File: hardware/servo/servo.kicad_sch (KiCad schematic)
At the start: 49 parts, among them J2 Conn_ARM_SWD_TagConnect_TC203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, U3 DRV8876PWPR, U4 STM32G030F6P6, U5 SIT3088EEUA, U6 SRV05-4

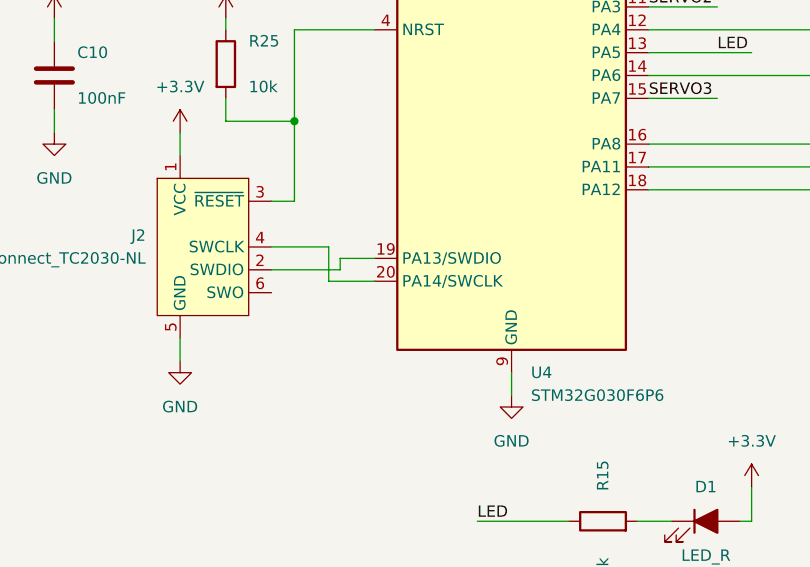
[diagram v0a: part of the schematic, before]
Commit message: hw/servo: add BOOT0 pull-down + test pad (same as ministepper)
STM32G030F6P6 on TSSOP-20 shares PA14 between SWCLK and the BOOT0
selector. Default option bytes read BOOT0 from the PA14 pin, so a
floating PA14 at cold boot (no debugger attached) can trigger an
unintended system-bootloader entry.

- R_BOOT0 (10k 0402, C25744) pull-down locks BOOT0 low at power-up
- TP_BOOT0 1x1mm solder pad for manual bootloader entry (short to
  +3V3 at reset to invoke system bootloader over USART1/RS-485 or
  I2C1)

Also embedded Connector:TestPoint in lib_symbols for BOM recognition.

Co-Authored-By: Claude Opus 4.6 (1M context) <noreply@anthropic.com>
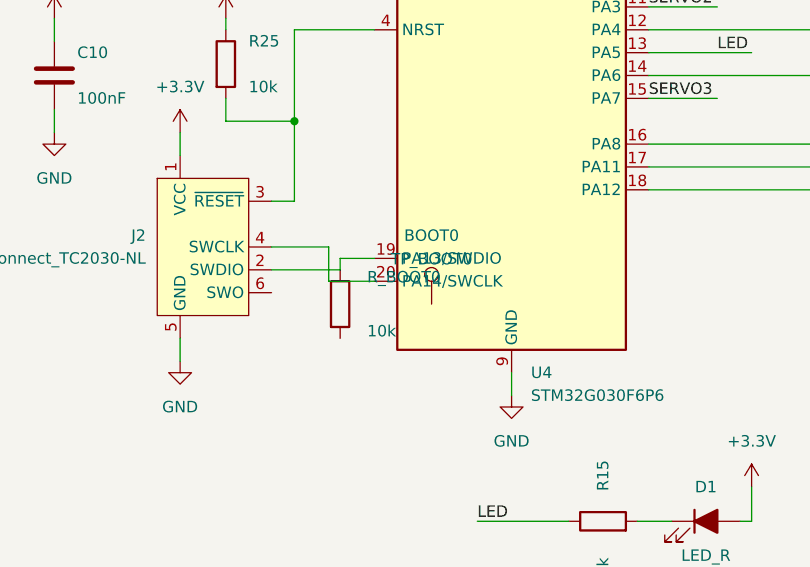
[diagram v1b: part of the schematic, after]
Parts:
- added R_BOOT0: 10k, Resistor_SMD:R_0402_1005Metric, symbol Device:R
- added TP_BOOT0: BOOT0, TestPoint:TestPoint_Pad_1.0x1.0mm, symbol Connector:TestPoint
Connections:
- net at J2.2 (SWDIO), U4.19 (PA13/SWDIO): now also R_BOOT0.1
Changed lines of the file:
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@@
+		)
+	)
+	(symbol
+		(lib_id "Device:R")
+		(at 201.93 166.37 0)
+		(unit 1)
+		(body_style 1)
+		(exclude_from_sim no)
+		(in_bom yes)
+		(on_board yes)
+		(in_pos_files yes)
+		(dnp no)
+		(uuid "b007bb01-1111-2222-3333-00000000r1ab")
+		(property "Reference" "R_BOOT0"
+			(at 204.93 163.37 0)
+			(show_name no)
+			(do_not_autoplace no)
+			(effects
+				(font
+					(size 1.27 1.27)
+				)
+				(justify left)
+			)
+		)
+		(property "Value" "10k"
+			(at 204.93 169.37 0)
+			(show_name no)
+			(do_not_autoplace no)
+			(effects
+				(font
+					(size 1.27 1.27)
+				)
+				(justify left)
+			)
+		)
+		(property "Footprint" "Resistor_SMD:R_0402_1005Metric"
+			(at 201.93 166.37 0)
+			(hide yes)
+			(show_name no)
+			(do_not_autoplace no)
+			(effects
+				(font
+					(size 1.27 1.27)
+				)
+			)
+		)
+		(property "Datasheet" ""
+			(at 201.93 166.37 0)
+			(hide yes)
+			(show_name no)
+			(do_not_autoplace no)
+			(effects
+				(font
+					(size 1.27 1.27)
+				)
+			)
+		)
+		(property "Description" "BOOT0 pull-down on PA14; locks cold boot to flash (BASIC)"
+			(at 201.93 166.37 0)
+			(hide yes)
+			(show_name no)
+			(do_not_autoplace no)
+			(effects
+				(font
+					(size 1.27 1.27)
+				)
+			)
+		)
+		(property "LCSC" "C25744"
+			(at 201.93 166.37 0)
+			(hide yes)
+			(show_name no)
+			(do_not_autoplace no)
+			(effects
+				(font
+					(size 1.27 1.27)
+				)
+			)
+		)
+		(property "MPN" "0402WGF1002TCE"
+			(at 201.93 166.37 0)
+			(hide yes)
+			(show_name no)
+			(do_not_autoplace no)
+			(effects
+				(font
+					(size 1.27 1.27)
+				)
+			)
+		)
+		(property "Manufacturer" "UNI-ROYAL"
+			(at 201.93 166.37 0)
+			(hide yes)
+			(show_name no)
+			(do_not_autoplace no)
+			(effects
+				(font
+					(size 1.27 1.27)
+				)
+			)
+		)
+		(pin "1"
+			(uuid "b007bb01-1111-2222-3333-00000000-pn01")
+		)
+		(pin "2"
+			(uuid "b007bb01-1111-2222-3333-00000000-pn02")
+		)
+		(instances
+			(project "servo"
+				(path "/e63e39d7-6ac0-4ffd-8aa3-1841a4541b55"
+					(reference "R_BOOT0")
+					(unit 1)
+				)
+			)
+		)
+	)
+	(symbol
+		(lib_id "Connector:TestPoint")
+		(at 212.09 166.37 0)
+		(unit 1)
+		(body_style 1)
+		(exclude_from_sim no)
+		(in_bom yes)
+		(on_board yes)
+		(in_pos_files yes)
+		(dnp no)
+		(uuid "b007bb02-1111-2222-3333-00000000tpab")
+		(property "Reference" "TP_BOOT0"
+			(at 212.09 161.37 0)
+			(show_name no)
+			(do_not_autoplace no)
+			(effects
+				(font
+					(size 1.27 1.27)
+				)
+			)
+		)
+		(property "Value" "BOOT0"
+			(at 212.09 158.75 0)
+			(show_name no)
+			(do_not_autoplace no)
+			(effects
+				(font
+					(size 1.27 1.27)
+				)
+			)
+		)
+		(property "Footprint" "TestPoint:TestPoint_Pad_1.0x1.0mm"
+			(at 212.09 166.37 0)
+			(hide yes)
+			(show_name no)
+			(do_not_autoplace no)
+			(effects
+				(font
+					(size 1.27 1.27)
+				)
+			)
+		)
+		(property "Datasheet" ""
+			(at 212.09 166.37 0)
+			(hide yes)
+			(show_name no)
+			(do_not_autoplace no)
+			(effects
+				(font
+					(size 1.27 1.27)
+				)
+			)
+		)
+		(property "Description" "Solder test point for manual BOOT0 select (short to +3V3 at reset)"
+			(at 212.09 166.37 0)
+			(hide yes)
+			(show_name no)
+			(do_not_autoplace no)
+			(effects
+				(font
+					(size 1.27 1.27)
+				)
+			)
+		)
+		(pin "1"
+			(uuid "b007bb02-1111-2222-3333-00000000-pn01")
+		)
+		(instances
+			(project "servo"
+				(path "/e63e39d7-6ac0-4ffd-8aa3-1841a4541b55"
+					(reference "TP_BOOT0")
+					(unit 1)
+				)
+			)
 		)
 	)

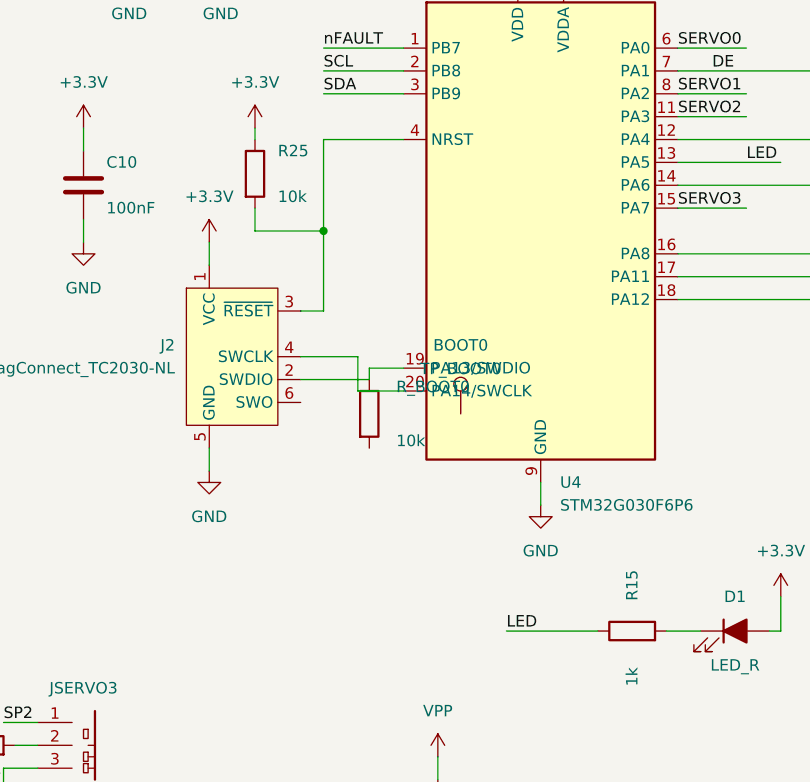
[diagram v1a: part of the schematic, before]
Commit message: hw+fw: fix STM32G071G8U6 UFQFPN28 symbol + pin map
The tsumikoro:STM32G071G8U6 symbol had a fabricated pin map that
didn't match ST DS12232 Figure 9 — VDD/VDDA were split onto pins 1/2
(they're actually fused on pin 3 on this package), NRST was assigned
to pin 3 (it's on pin 5), pin 28 was labelled VDD_2 (it's PB8), and
DIR2 was on PB2 (which is not bonded out on UFQFPN28).

Because the ministepper is not yet wired and firmware addresses GPIOs
by port name, no PCB damage resulted — but every pin number in docs,
firmware comments, and the symbol was off.

Rewritten against the datasheet:

- Symbol rebuilt with the real 29-pin UFQFPN28 layout (28 signal +
  EP), including PC14/PC15 on pins 1/2 and PC6 on pin 17.
- DIR2 reassigned from phantom PB2 to PC6 (pin 17).
- GPIOC clock enabled in firmware for PC6.
- CLAUDE.md and ministepper/docs/README.md pin tables rewritten.
- docs/README now calls out required MCU decoupling (100 nF + 4.7 µF
  bulk + NRST filter) that was implicitly missing when docs assumed
  two separate VDD pins.

Co-Authored-By: Claude Opus 4.6 (1M context) <noreply@anthropic.com>
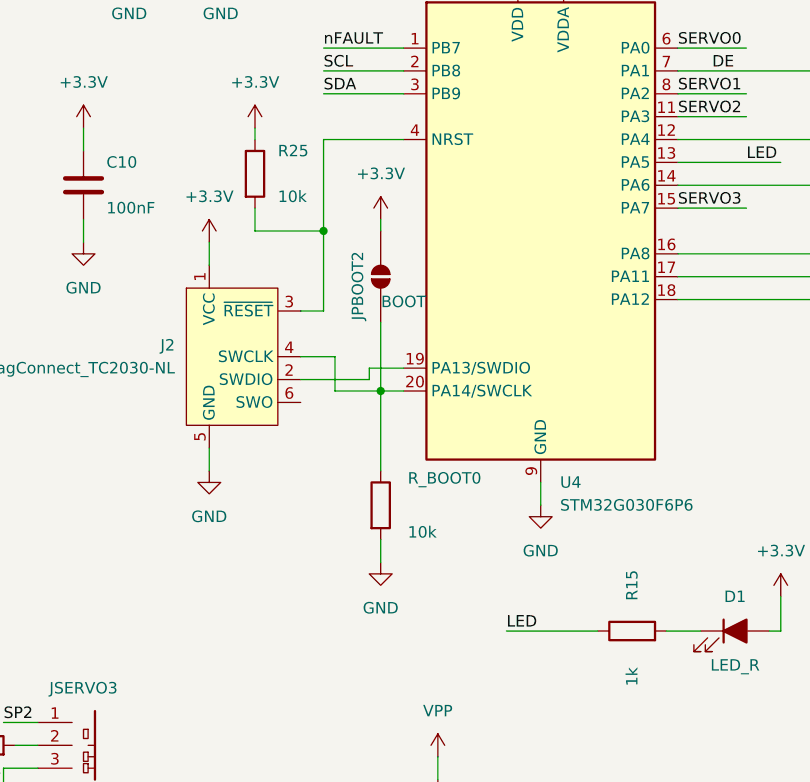
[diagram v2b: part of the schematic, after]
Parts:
- removed TP_BOOT0: BOOT0, TestPoint:TestPoint_Pad_1.0x1.0mm, symbol Connector:TestPoint
- added JPBOOT2: BOOT, Jumper:SolderJumper-2_P1.3mm_Open_Pad1.0x1.5mm, symbol Jumper:SolderJumper_2_Open
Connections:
- net +3.3V: now also JPBOOT2.2 (B)
- net GND: now also R_BOOT0.2
- net at J2.2 (SWDIO), U4.19 (PA13/SWDIO): no longer R_BOOT0.1
- net at J2.4 (SWCLK), U4.20 (PA14/SWCLK): now also R_BOOT0.1, JPBOOT2.1 (A)

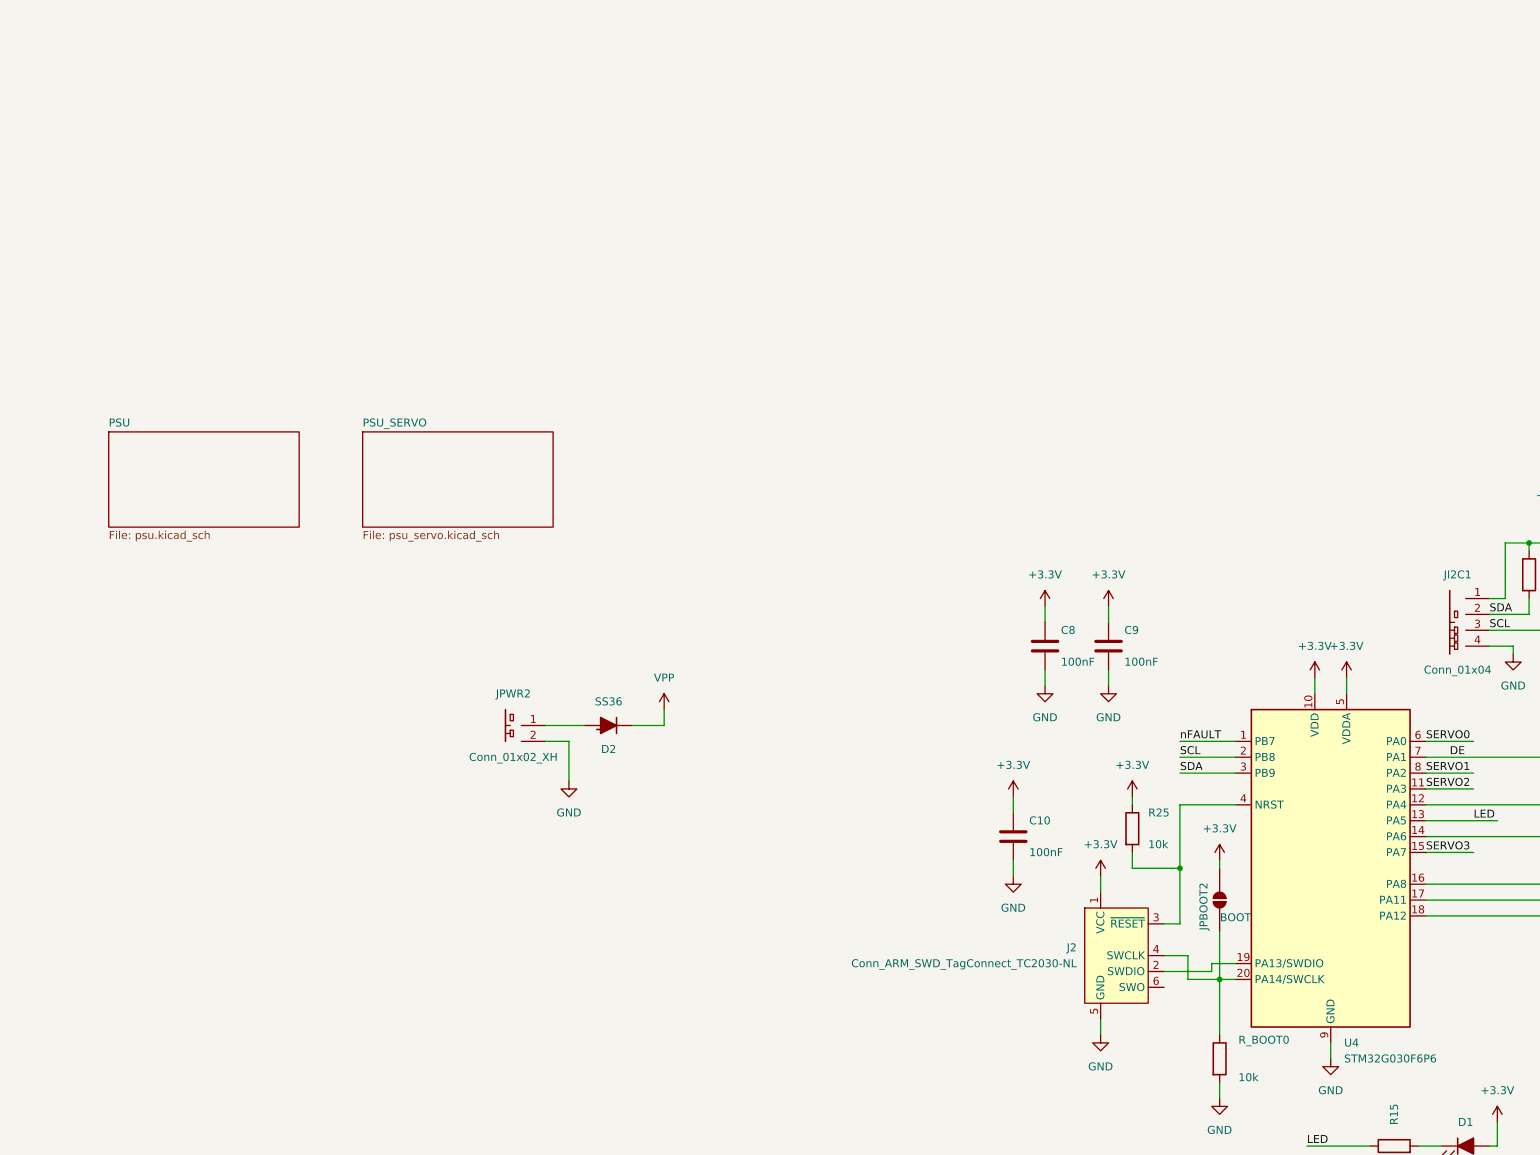
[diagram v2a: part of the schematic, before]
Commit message: hw/servo: rev 0.1 DO-NOT-FAB; rewrite G030F6P6 symbol for rev 0.2
The tsumikoro:STM32G030F6P6 symbol had a fabricated pinout that did
not match ST DS12991 Figure 4 / Table 12 — VDD/VDDA were split
(they're fused on pad 4), VSS was at pad 9 (it's pad 5), NRST was at
pad 4 (it's pad 6), and every GPIO was shifted. The existing
schematic wiring and PCB routing followed the fake symbol, so rev 0.1
as-drawn would short +3V3 to GND through pad 5 and never power the
MCU.

Decision: do not fab rev 0.1. Respin as rev 0.2 with the same chip
(G030F6P6 TSSOP20) and correct pinout. User will re-wire the
schematic + re-route the PCB in KiCad.

Changes in this commit:

- Rewrote the STM32G030F6P6 symbol (both master lib and the embedded
  copy in servo.kicad_sch) to the real pinout. This breaks the
  existing wires — intentional, since the board must be redone.
- Added a prominent (text) block on servo.kicad_sch enumerating the
  intended per-pad wiring for rev 0.2 so the rework is straightforward.
- Dropped PB7 nFAULT from the design: pad 1 bonds PB7 and PB8 to the
  same net, so only one can be used — PB8 wins for I2C1 SCL. nFAULT
  monitoring must be handled in firmware (current sense / timeout).
- CLAUDE.md servo section rewritten with correct pin map and a loud
  rev-0.1 warning.
- Firmware Read_Hardware_ID() marked dead (pad 1 can no longer expose
  two independent straps).

Ministepper G071 fix from a80dd6d is unaffected.

Co-Authored-By: Claude Opus 4.6 (1M context) <noreply@anthropic.com>
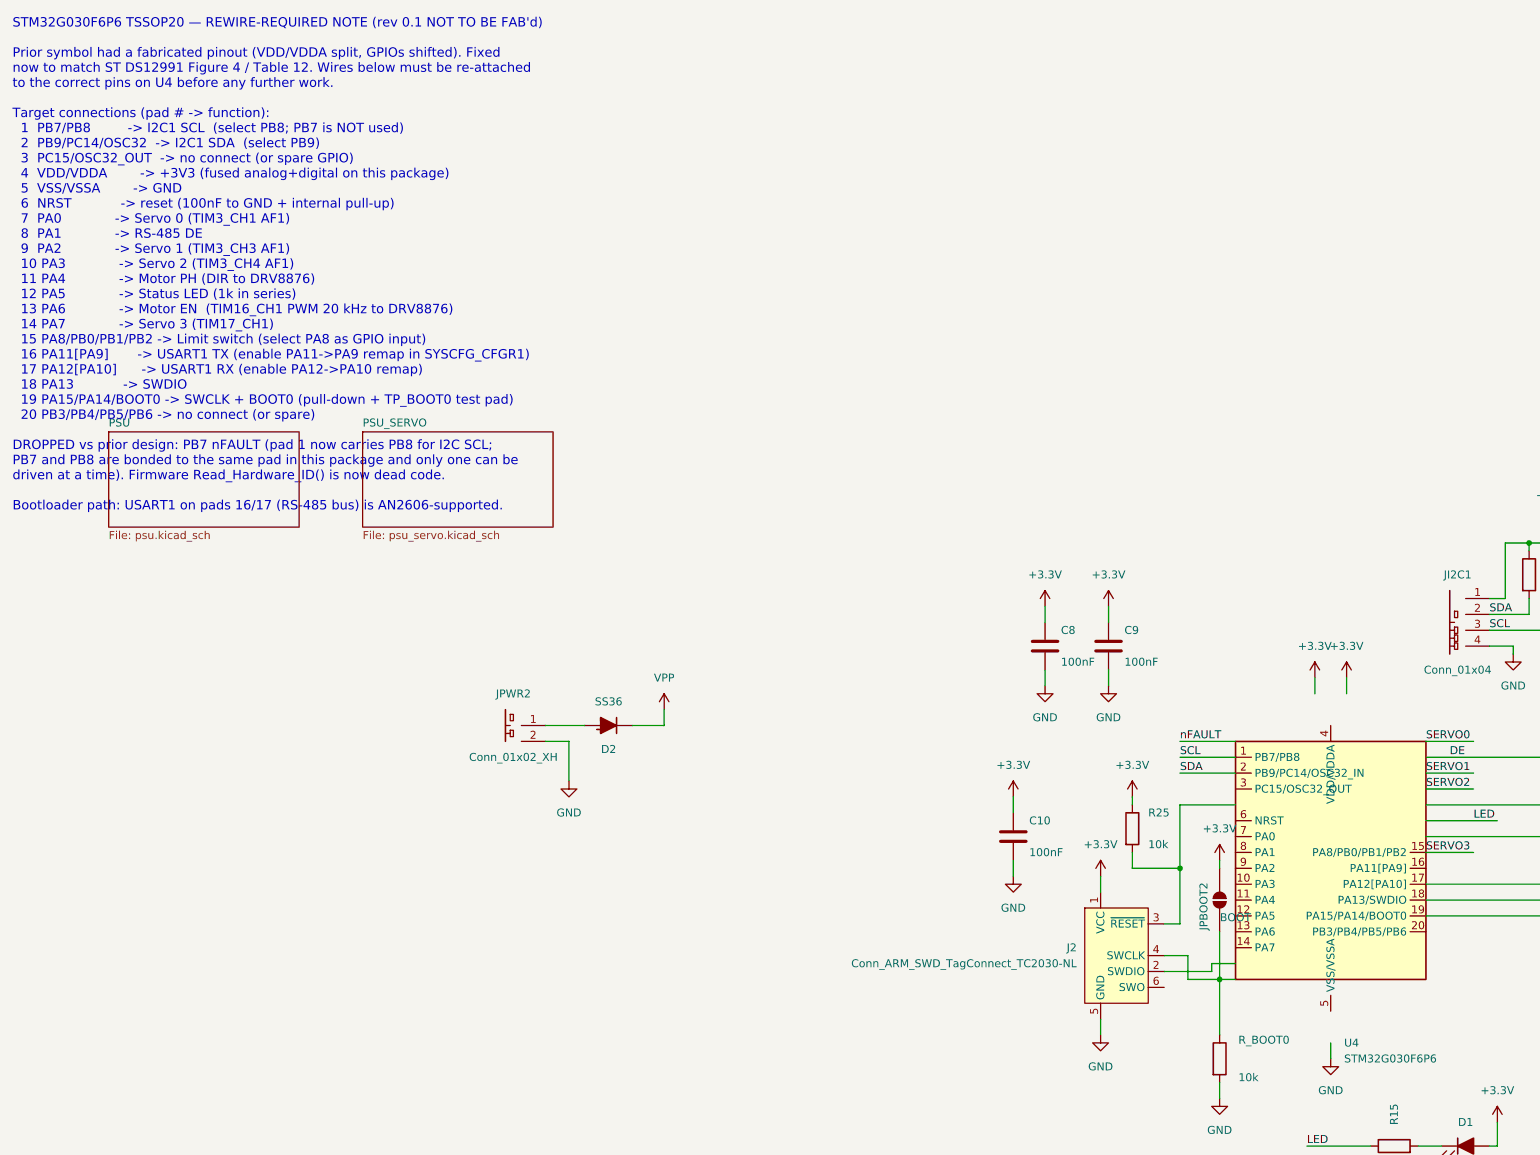
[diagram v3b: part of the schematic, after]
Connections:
- net +3.3V: no longer U4.10 (VDD), U4.5 (VDDA)
- net DE: no longer U4.7 (PA1)
- net GND: no longer U4.9 (GND)
- net LED: no longer U4.13 (PA5)
- net SCL: now also U4.1 (PB7/PB8); no longer U4.2 (PB8)
- net SDA: now also U4.2 (PB9/PC14/OSC32_IN); no longer U4.3 (PB9)
- net SERVO0: no longer U4.6 (PA0)
- net SERVO1: no longer U4.8 (PA2)
- net SERVO2: no longer U4.11 (PA3)
- net nFAULT: no longer U4.1 (PB7)
- net at J2.2 (SWDIO): no longer U4.19 (PA13/SWDIO)
- net at J2.3 (~{RESET}), R25.2: no longer U4.4 (NRST)
- net at J2.4 (SWCLK), JPBOOT2.1 (A), R_BOOT0.1: no longer U4.20 (PA14/SWCLK)
- net at U4.12 (PA5): no longer U3.2 (PH/IN2)
- net at U4.14 (PA7): no longer U3.1 (EN/IN1)
- net at JLIM2.1 (Pin_1), R20.2: now also U4.17 (PA12[PA10]); no longer U4.16 (PA8)
- net at U5.4 (DI): now also U4.18 (PA13/SWDIO); no longer U4.17 (PA11)
- net at U5.1 (RO): now also U4.19 (PA15/PA14/BOOT0); no longer U4.18 (PA12)
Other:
- note added: "STM32G030F6P6 TSSOP20 — REWIRE-REQUIRED NOTE (rev 0.1 NOT TO BE FAB'd) Prior symbol had a fabricated pinout (VDD/VDDA split, GPIOs shifted). Fixed now to match ST DS12991 Figure 4 / Table 12. Wires below must be re-attached to the correct pins on U4 before any further work. Target connections (pad # -> function): 1 PB7/PB8 -> I2C1 SCL (select PB8; PB7 is NOT used) 2 PB9/PC14/OSC32 -> I2C1 SDA (se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"
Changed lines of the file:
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@@
 		)
+	)
+	(text "STM32G030F6P6 TSSOP20 — REWIRE-REQUIRED NOTE (rev 0.1 NOT TO BE FAB'd)\n\nPrior symbol had a fabricated pinout (VDD/VDDA split, GPIOs shifted). Fixed\nnow to match ST DS12991 Figure 4 / Table 12. Wires below must be re-attached\nto the correct pins on U4 before any further work.\n\nTarget connections (pad # -> function):\n  1  PB7/PB8         -> I2C1 SCL  (select PB8; PB7 is NOT used)\n  2  PB9/PC14/OSC32  -> I2C1 SDA  (select PB9)\n  3  PC15/OSC32_OUT  -> no connect (or spare GPIO)\n  4  VDD/VDDA        -> +3V3 (fused analog+digital on this package)\n  5  VSS/VSSA        -> GND\n  6  NRST            -> reset (100nF to GND + internal pull-up)\n  7  PA0             -> Servo 0 (TIM3_CH1 AF1)\n  8  PA1             -> RS-485 DE\n  9  PA2             -> Servo 1 (TIM3_CH3 AF1)\n  10 PA3             -> Servo 2 (TIM3_CH4 AF1)\n  11 PA4             -> Motor PH (DIR to DRV8876)\n  12 PA5             -> Status LED (1k in series)\n  13 PA6             -> Motor EN  (TIM16_CH1 PWM 20 kHz to DRV8876)\n  14 PA7             -> Servo 3 (TIM17_CH1)\n  15 PA8/PB0/PB1/PB2 -> Limit switch (select PA8 as GPIO input)\n  16 PA11[PA9]       -> USART1 TX (enable PA11->PA9 remap in SYSCFG_CFGR1)\n  17 PA12[PA10]      -> USART1 RX (enable PA12->PA10 remap)\n  18 PA13            -> SWDIO\n  19 PA15/PA14/BOOT0 -> SWCLK + BOOT0 (pull-down + TP_BOOT0 test pad)\n  20 PB3/PB4/PB5/PB6 -> no connect (or spare)\n\nDROPPED vs prior design: PB7 nFAULT (pad 1 now carries PB8 for I2C SCL;\nPB7 and PB8 are bonded to the same pad in this package and only one can be\ndriven at a time). Firmware Read_Hardware_ID() is now dead code.\n\nBootloader path: USART1 on pads 16/17 (RS-485 bus) is AN2606-supported.\n"
+		(exclude_from_sim no)
+		(at 10 10 0)
+		(effects
+			(font
+				(size 1.5 1.5)
+			)
+			(justify left top)
+		)
+		(uuid "11110000-aaaa-bbbb-cccc-000servo0001")
 	)
 	(sheet_instances
